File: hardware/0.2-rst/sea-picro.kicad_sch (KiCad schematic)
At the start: 54 parts, among them J1 USB_C_Receptacle_USB2.0, J2 0.1" x 12, J3 0.1" x 12, J4 D+, J5 D-, J6 0.1" x 5, Q1 2N7002VC-7, Q2 2N7002VC-7, U1 ME6211C33M5G-N, U2 GD25Q64CWIGR, U3 RP2040, Y1 12MHz

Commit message: split into rst and ext versionN
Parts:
- removed J6: 0.1" x 5, josh-connectors:PinHeader_1x05_P2.54mm_Circle, symbol Connector:Conn_01x05_Male
- added SW1: SWITCH, josh-buttons-switches:SW_Push_KMR2, symbol Switch:SW_Push
- added TP3: BOOT, TestPoint:TestPoint_Pad_D1.0mm, symbol Connector:TestPoint
- added TP4: CLK, josh-test-point:TestPoint_THTPad_D1.0mm_Drill0.5mm_NO_SILK, symbol Connector:TestPoint
- added TP5: IO, josh-test-point:TestPoint_THTPad_D1.0mm_Drill0.5mm_NO_SILK, symbol Connector:TestPoint
- TP1: value CLK -> nRST; footprint josh-test-point:TestPoint_THTPad_D1.0mm_Drill0.5mm_NO_SILK -> TestPoint:TestPoint_Pad_D1.0mm
- TP2: value IO -> DELAY; footprint josh-test-point:TestPoint_THTPad_D1.0mm_Drill0.5mm_NO_SILK -> TestPoint:TestPoint_Pad_D1.0mm
- Y1: LCSC C2C2149204149205 -> C2149204
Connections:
- net BOOT: now also TP3.1
- net GND: now also SW1.1
- net SWDCLK: now also TP4.1; no longer TP1.1
- net SWDIO: now also TP5.1; no longer TP2.1
- net SWITCH: now also SW1.2
- net nRST: now also TP1.1
- net at C19.1, C5.1, Q2.5 (G)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: now also TP2.1
- net 10: no longer names the net of U3.13 (GPIO10)
- net 11: no longer names the net of U3.14 (GPIO11)
- net 15: no longer names the net of U3.15 (GPIO12)
- net 18: no longer names the net of U3.29 (GPIO18)
- net 19: no longer names the net of U3.30 (GPIO19)
- no-connect marks 7 -> 12
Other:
- title: Sea Picro Extended -> Sea Picro Reset

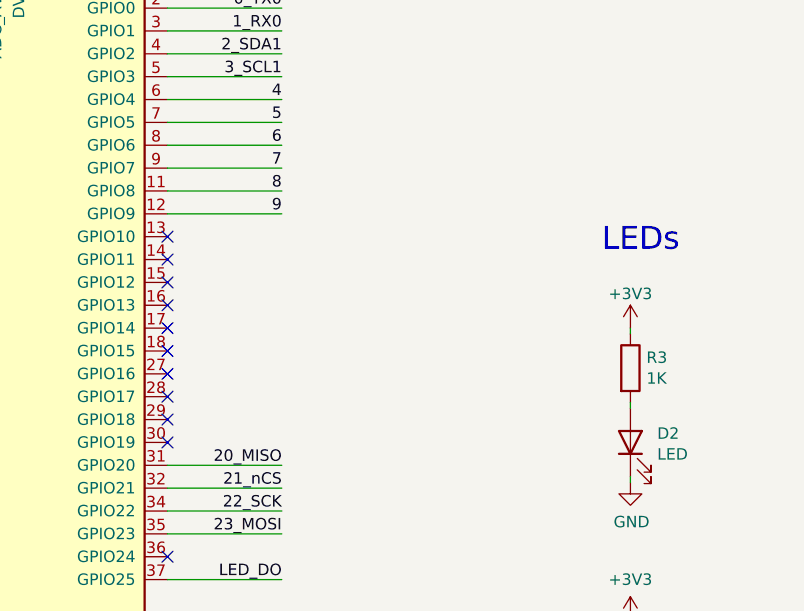
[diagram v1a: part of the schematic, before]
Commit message: add usb vbus detect
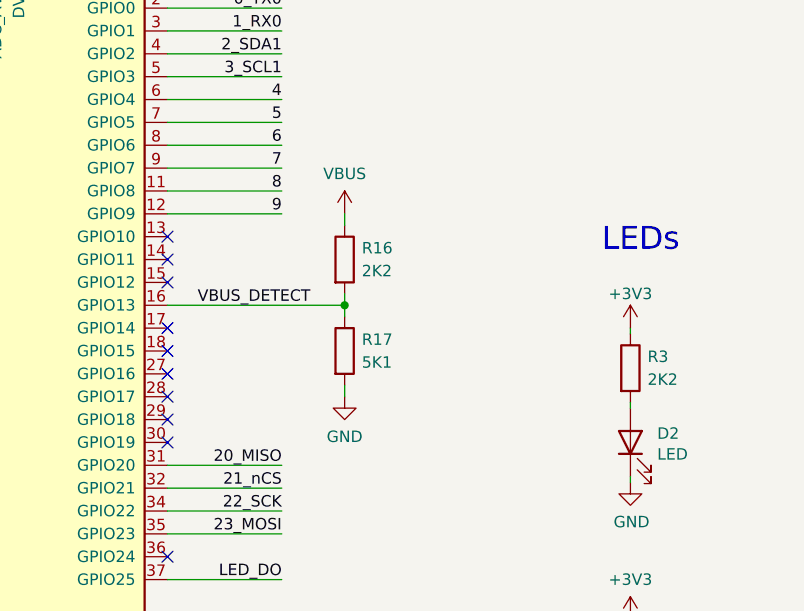
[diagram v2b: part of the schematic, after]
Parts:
- added R16: 2K2, Resistor_SMD:R_0402_1005Metric, symbol Device:R
- added R17: 5K1, Resistor_SMD:R_0402_1005Metric, symbol Device:R
- R3: value 1K -> 2K2; LCSC C11702 -> C25879; MPN  0402WGF1001TCE -> 0402WGF2201TCE
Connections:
- net GND: now also R17.2
- net VBUS: now also R16.1
- net VBUS_DETECT: now reaches U3.16 (GPIO13)
- net VBUS_DETECT: now also R16.2, R17.1
- no-connect marks 12 -> 11

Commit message: add LED driver and more test points
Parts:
- TP1, TP2, TP3: footprint TestPoint:TestPoint_Pad_D1.0mm -> josh-test-point:TestPoint_SMDPad_D1.0mm_NO_SILK
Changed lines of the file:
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@@
       (effects (font (size 1.27 1.27)) (justify left))
     )
-    (property "Footprint" "TestPoint:TestPoint_Pad_D1.0mm" (id 2) (at 121.92 173.355 0)
+    (property "Footprint" "josh-test-point:TestPoint_SMDPad_D1.0mm_NO_SILK" (id 2) (at 121.92 173.355 0)
       (effects (font (size 1.27 1.27)) hide)
     )
@@
       (effects (font (size 1.27 1.27)) (justify left))
     )
-    (property "Footprint" "TestPoint:TestPoint_Pad_D1.0mm" (id 2) (at 73.025 155.575 0)
+    (property "Footprint" "josh-test-point:TestPoint_SMDPad_D1.0mm_NO_SILK" (id 2) (at 73.025 155.575 0)
       (effects (font (size 1.27 1.27)) hide)
     )
@@
       (effects (font (size 1.27 1.27)) (justify left))
     )
-    (property "Footprint" "TestPoint:TestPoint_Pad_D1.0mm" (id 2) (at 109.22 174.625 0)
+    (property "Footprint" "josh-test-point:TestPoint_SMDPad_D1.0mm_NO_SILK" (id 2) (at 109.22 174.625 0)
       (effects (font (size 1.27 1.27)) hide)
     )
@@
     )
     (path "/2b41e7a9-0c09-4e41-9f7a-61ea0174a7da"
-      (reference "TP1") (unit 1) (value "nRST") (footprint "TestPoint:TestPoint_Pad_D1.0mm")
+      (reference "TP1") (unit 1) (value "nRST") (footprint "josh-test-point:TestPoint_SMDPad_D1.0mm_NO_SILK")
     )
     (path "/6932f11f-ad59-4756-a526-ea6bfbb8b520"
-      (reference "TP2") (unit 1) (value "DELAY") (footprint "TestPoint:TestPoint_Pad_D1.0mm")
+      (reference "TP2") (unit 1) (value "DELAY") (footprint "josh-test-point:TestPoint_SMDPad_D1.0mm_NO_SILK")
     )
     (path "/02975932-bf30-4606-900b-744ae844a718"
-      (reference "TP3") (unit 1) (value "BOOT") (footprint "TestPoint:TestPoint_Pad_D1.0mm")
+      (reference "TP3") (unit 1) (value "BOOT") (footprint "josh-test-point:TestPoint_SMDPad_D1.0mm_NO_SILK")
     )
     (path "/da9d8c97-5301-4179-9d57-0a9ed815b1de"

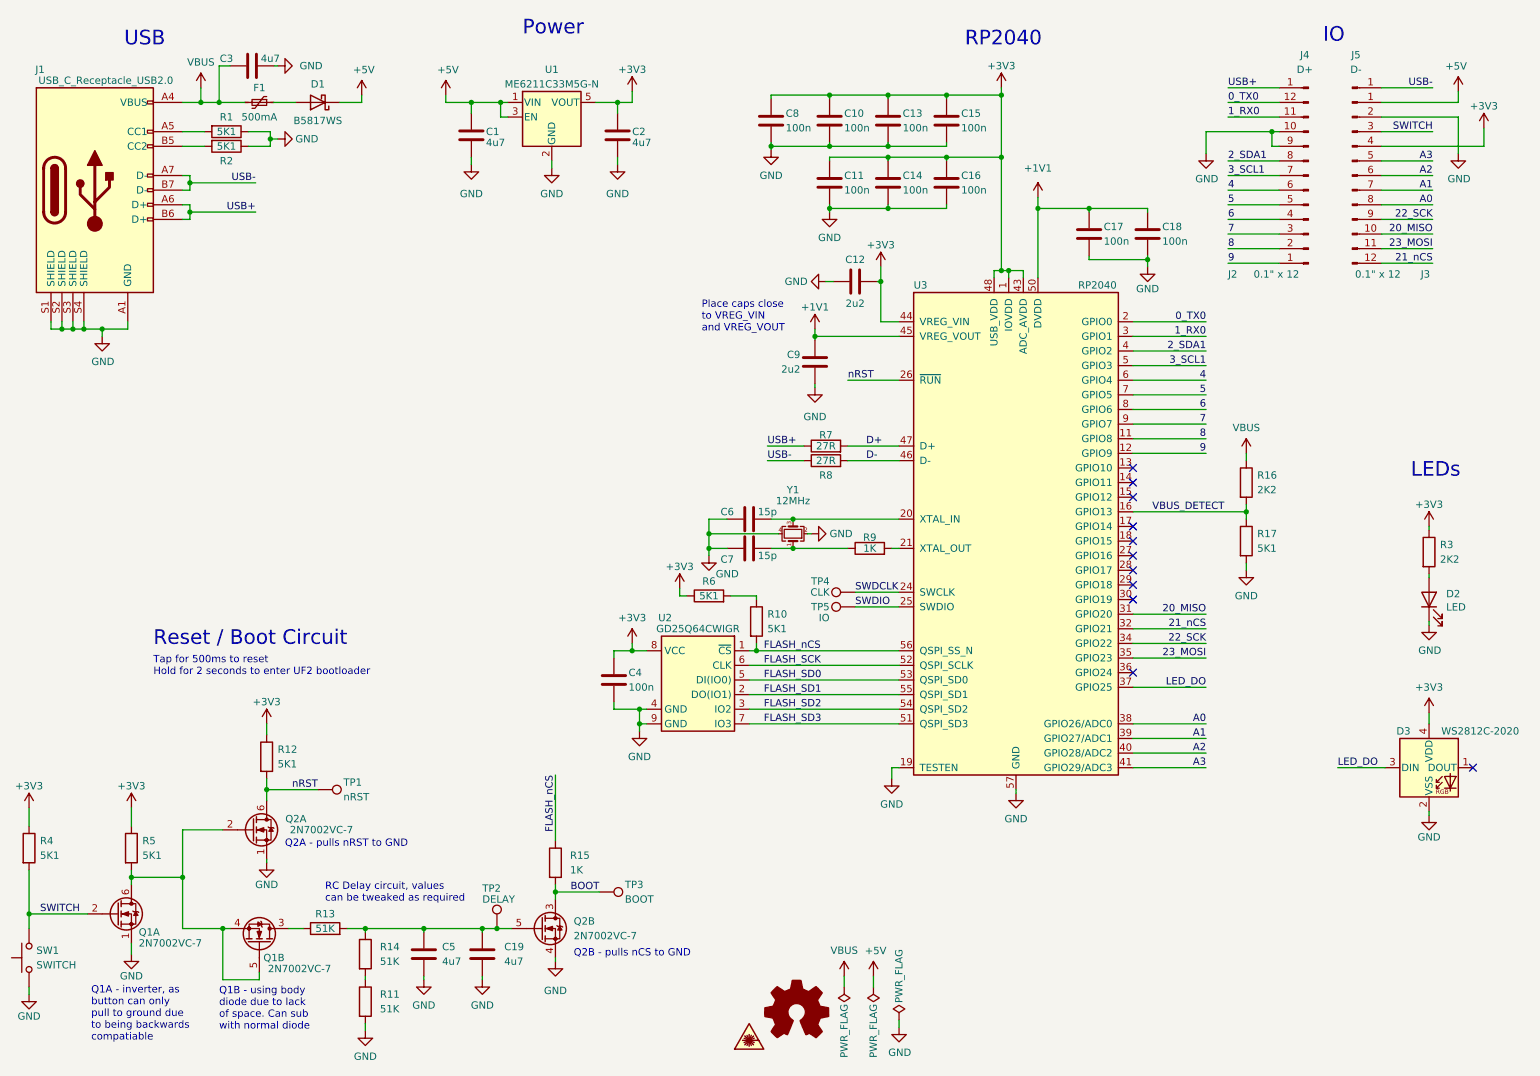
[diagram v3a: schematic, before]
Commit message: update ldo caps to 1u
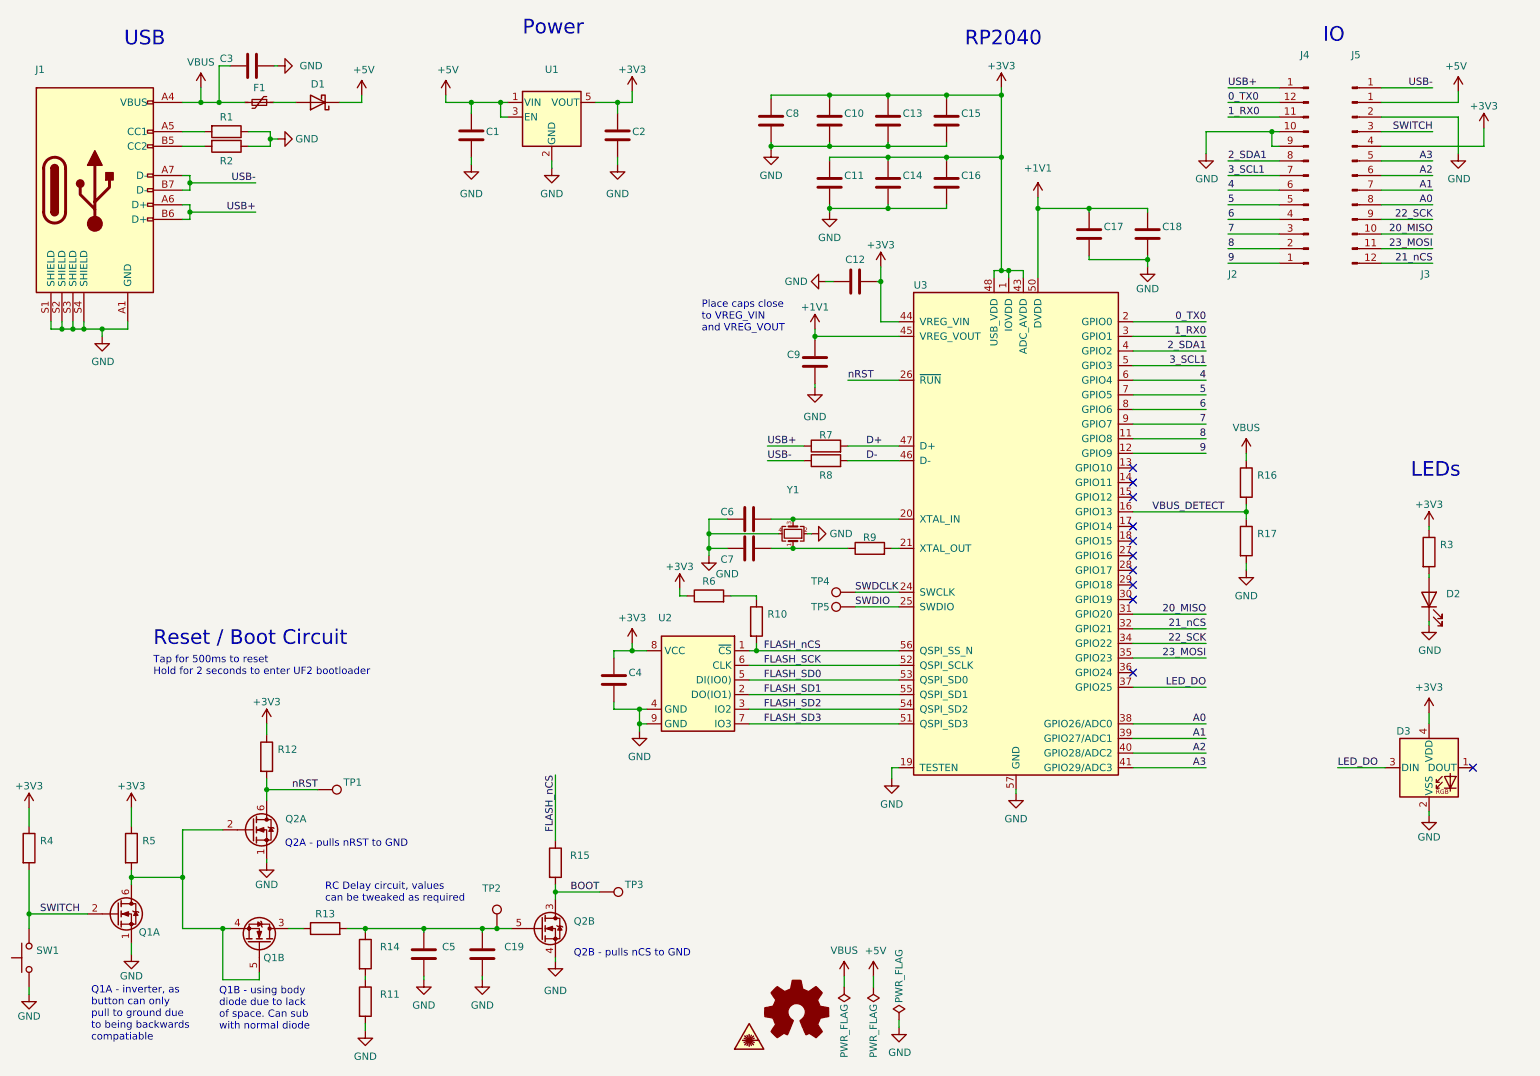
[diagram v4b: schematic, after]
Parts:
- C1, C19, C2, C3, C5: value 4u7 -> (none); footprint Capacitor_SMD:C_0402_1005Metric -> (none)
- C10, C11, C13, C14, C15, C16, C17, C18, C4, C8: value 100n -> (none); footprint Capacitor_SMD:C_0402_1005Metric -> (none)
- C12, C9: value 2u2 -> (none); footprint Capacitor_SMD:C_0402_1005Metric -> (none); LCSC C12530 -> C15849; MPN  CL05A225MQ5NSNC -> CL10A105KB8NNNC
- C6, C7: value 15p -> (none); footprint Capacitor_SMD:C_0402_1005Metric -> (none)
- D1: value B5817WS -> (none); footprint Diode_SMD:D_SOD-323 -> (none)
- D2: value LED -> (none); footprint LED_SMD:LED_0603_1608Metric -> (none)
- D3: value WS2812C-2020 -> (none); footprint josh-led:WS2812C-2020 -> (none)
- F1: value 500mA -> (none); footprint josh-passives-smt:Fuse_0603_1608Metric -> (none)
- J1: value USB_C_Receptacle_USB2.0 -> (none); footprint josh-connectors:USB-C_MID_MOUNT_918-418K2024S40000 -> (none)
- J2, J3: value 0.1" x 12 -> (none); footprint josh-connectors:Castellated_Short_P2.54x12 -> (none)
- J4: value D+ -> (none); footprint josh-connectors:PinHeader_1x01_P2.54mm_Circle -> (none)
- J5: value D- -> (none); footprint josh-connectors:PinHeader_1x01_P2.54mm_Circle -> (none)
- LOGO1: value Logo_Open_Hardware_Small -> (none); footprint josh-logos:OSHW_Logo_3.6x3.6_F.Mask -> (none)
- LOGO2: value Sea-Picro -> (none); footprint josh-logos:sea-picro-silk -> (none)
- Q1, Q2: value 2N7002VC-7 -> (none); footprint Package_TO_SOT_SMD:SOT-563 -> (none)
- R1, R10, R12, R17, R2, R4, R5, R6: value 5K1 -> (none); footprint Resistor_SMD:R_0402_1005Metric -> (none)
- R11, R13, R14: value 51K -> (none); footprint Resistor_SMD:R_0402_1005Metric -> (none)
- R15, R9: value 1K -> (none); footprint Resistor_SMD:R_0402_1005Metric -> (none)
- R16, R3: value 2K2 -> (none); footprint Resistor_SMD:R_0402_1005Metric -> (none)
- R7, R8: value 27R -> (none); footprint Resistor_SMD:R_0402_1005Metric -> (none)
- SW1: value SWITCH -> (none); footprint josh-buttons-switches:SW_Push_KMR2 -> (none)
- TP1: value nRST -> (none); footprint josh-test-point:TestPoint_SMDPad_D1.0mm_NO_SILK -> (none)
- TP2: value DELAY -> (none); footprint josh-test-point:TestPoint_SMDPad_D1.0mm_NO_SILK -> (none)
- TP3: value BOOT -> (none); footprint josh-test-point:TestPoint_SMDPad_D1.0mm_NO_SILK -> (none)
- TP4: value CLK -> (none); footprint josh-test-point:TestPoint_THTPad_D1.0mm_Drill0.5mm_NO_SILK -> (none)
- TP5: value IO -> (none); footprint josh-test-point:TestPoint_THTPad_D1.0mm_Drill0.5mm_NO_SILK -> (none)
- U1: value ME6211C33M5G-N -> (none); footprint Package_TO_SOT_SMD:SOT-23-5 -> (none)
- U2: value GD25Q64CWIGR -> (none); footprint Package_SON:WSON-8-1EP_6x5mm_P1.27mm_EP3.4x4mm -> (none)
- U3: value RP2040 -> (none); footprint josh-dfn-qfn:RP2040-QFN-56 -> (none)
- Y1: value 12MHz -> (none); footprint josh-oscillators:Crystal_SMD_2520-4Pin_2.5x2.0mm -> (none)

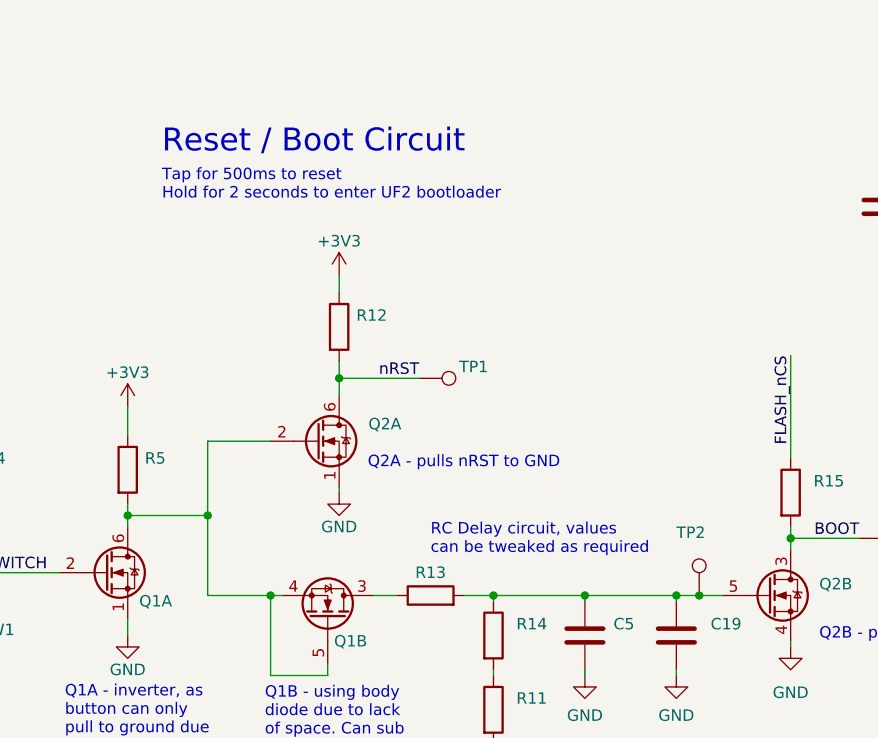
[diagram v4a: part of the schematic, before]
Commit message: fixes after assembly
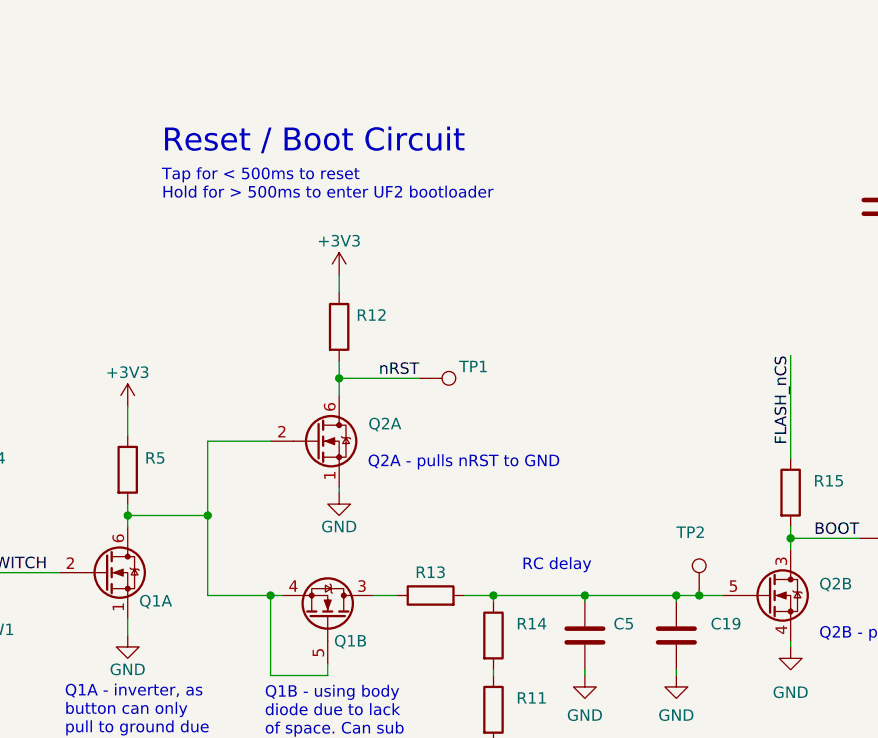
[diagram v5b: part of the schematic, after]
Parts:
- U1: LCSC C82942 -> C150742; MPN  ME6211C33M5G-N -> AP7365-33WG-7; Manufacturer MICRONE(Nanjing Micro One Elec) -> Diodes Incorporated
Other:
- note added: "RC delay"
- note added: "Tap for < 500ms to reset Hold for > 500ms to enter UF2 bootloader"
- note removed: "RC Delay circuit, values can be tweaked as required"
- note removed: "Tap for 500ms to reset Hold for 2 seconds to enter UF2 bootloader"
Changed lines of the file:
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@@
     (effects (font (size 1.27 1.27)) (justify left bottom))
   )
-  (text "Tap for 500ms to reset\nHold for 2 seconds to enter UF2 bootloader"
+  (text "Tap for < 500ms to reset\nHold for > 500ms to enter UF2 bootloader"
     (at 44.45 130.81 0)
     (effects (font (size 1.27 1.27)) (justify left bottom))
   )
-  (text "RC Delay circuit, values\ncan be tweaked as required"
-    (at 74.295 170.18 0)
+  (text "RC delay" (at 84.455 172.085 0)
     (effects (font (size 1.27 1.27)) (justify left bottom))
   )
@@
       (effects (font (size 1.27 1.27)) hide)
     )
-    (property "LCSC" "C82942" (id 4) (at 113.665 33.655 0)
-      (effects (font (size 1.27 1.27)) hide)
-    )
-    (property "MPN " "ME6211C33M5G-N" (id 5) (at 113.665 33.655 0)
-      (effects (font (size 1.27 1.27)) hide)
-    )
-    (property "Manufacturer" "MICRONE(Nanjing Micro One Elec)" (id 6) (at 113.665 33.655 0)
+    (property "LCSC" "C150742" (id 4) (at 113.665 33.655 0)
+      (effects (font (size 1.27 1.27)) hide)
+    )
+    (property "MPN " "AP7365-33WG-7 " (id 5) (at 113.665 33.655 0)
+      (effects (font (size 1.27 1.27)) hide)
+    )
+    (property "Manufacturer" "Diodes Incorporated" (id 6) (at 113.665 33.655 0)
       (effects (font (size 1.27 1.27)) hide)
     )
@@
     )
     (path "/d26fce45-c1d6-42bc-931d-972bf3799097"
-      (reference "U1") (unit 1) (value "ME6211C33M5G-N") (footprint "Package_TO_SOT_SMD:SOT-23-5")
+      (reference "U1") (unit 1) (value "AP7365-33WG-7 ") (footprint "Package_TO_SOT_SMD:SOT-23-5")
     )
     (path "/578f7d98-6025-491f-b2c7-18b0b10fb26e"
